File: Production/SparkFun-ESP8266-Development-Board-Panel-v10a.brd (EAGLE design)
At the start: 192.3 x 198.1 mm, 1515 parts, among them J1 DNP, J10 DNP, J11 DNP, J12 DNP, J13 DNP, J14 DNP, J15 DNP, J16 DNP, J17 DNP, J18 DNP, J19 DNP, J2 DNP, J20 DNP, J21 DNP, J3 DNP, J4 DNP, J5 DNP, J6 DNP, J7 DNP, J8 DNP, J9 DNP, Q1 2.5A/30V, Q10 2.5A/30V, Q11 2.5A/30V, Q12 2.5A/30V, Q13 2.5A/30V, Q14 2.5A/30V, Q15 2.5A/30V, Q16 2.5A/30V, Q17 2.5A/30V, Q18 2.5A/30V, Q19 2.5A/30V, Q2 2.5A/30V, Q20 2.5A/30V, Q21 2.5A/30V, Q3 2.5A/30V, Q4 2.5A/30V, Q5 2.5A/30V, Q6 2.5A/30V, Q7 2.5A/30V, Q8 2.5A/30V, Q9 2.5A/30V, U1 ESP8266, U10 ATECC108-MAHDA, U100 AT25SF041-SOIC8, U101 ATECC108-MAHDA, U102 MCP73831, U103 AP2112K-3.3V, U104 TMP1021:1, U105 TSL2561FN, U106 ESP8266, U107 AT25SF041-SOIC8, U108 ATECC108-MAHDA, U109 MCP73831, U11 MCP73831, U110 AP2112K-3.3V, U111 TMP1021:1, U112 TSL2561FN, U113 ESP8266, U114 AT25SF041-SOIC8, U115 ATECC108-MAHDA, U116 MCP73831, U117 AP2112K-3.3V, U118 TMP1021:1, U119 TSL2561FN, U12 AP2112K-3.3V, U120 ESP8266, U121 AT25SF041-SOIC8, U122 ATECC108-MAHDA, U123 MCP73831, U124 AP2112K-3.3V, U125 TMP1021:1, U126 TSL2561FN, U127 ESP8266, U128 AT25SF041-SOIC8, U129 ATECC108-MAHDA, U13 TMP1021:1, U130 MCP73831, U131 AP2112K-3.3V, U132 TMP1021:1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

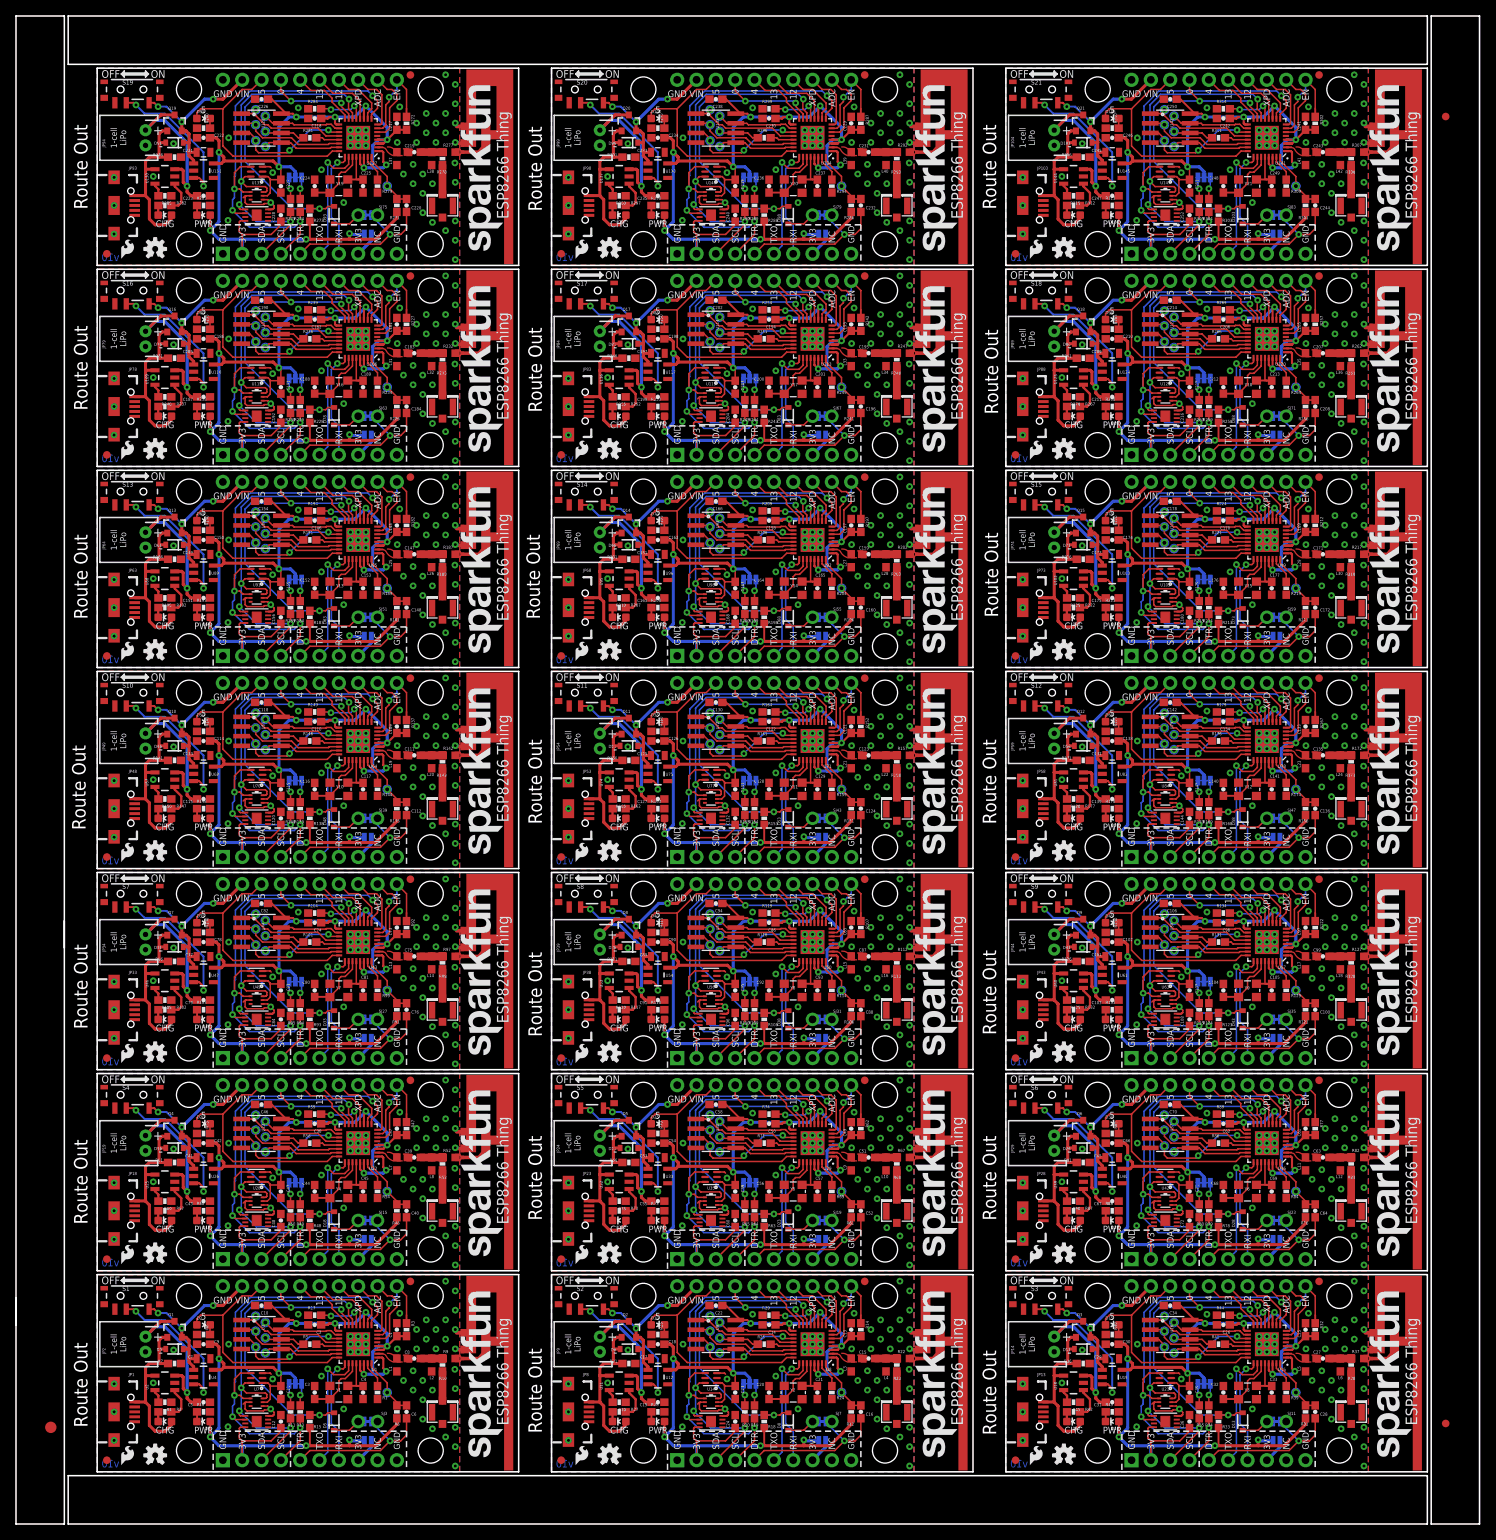
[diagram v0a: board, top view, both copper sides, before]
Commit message: Fix Silkscreen and Copper Width 0 Issue
- Replace Silkscreen for SparkFun, SFE Flame, OSH logo, and RF antenna on individual board and panel with current packages from the SparkFun Eagle Library. By having a defined width for the silkscreen/copper (instead of a "0" width), the CAM job does not generate an "infinite" amount of lines for the polygon => [ [https://learn.sparkfun.com/tutorials/importing-custom-images-into-eagle/#method-1-svg-to-polygon](https://learn.sparkfun.com/tutorials/importing-custom-images-into-eagle/#method-1-svg-to-polygon) ].
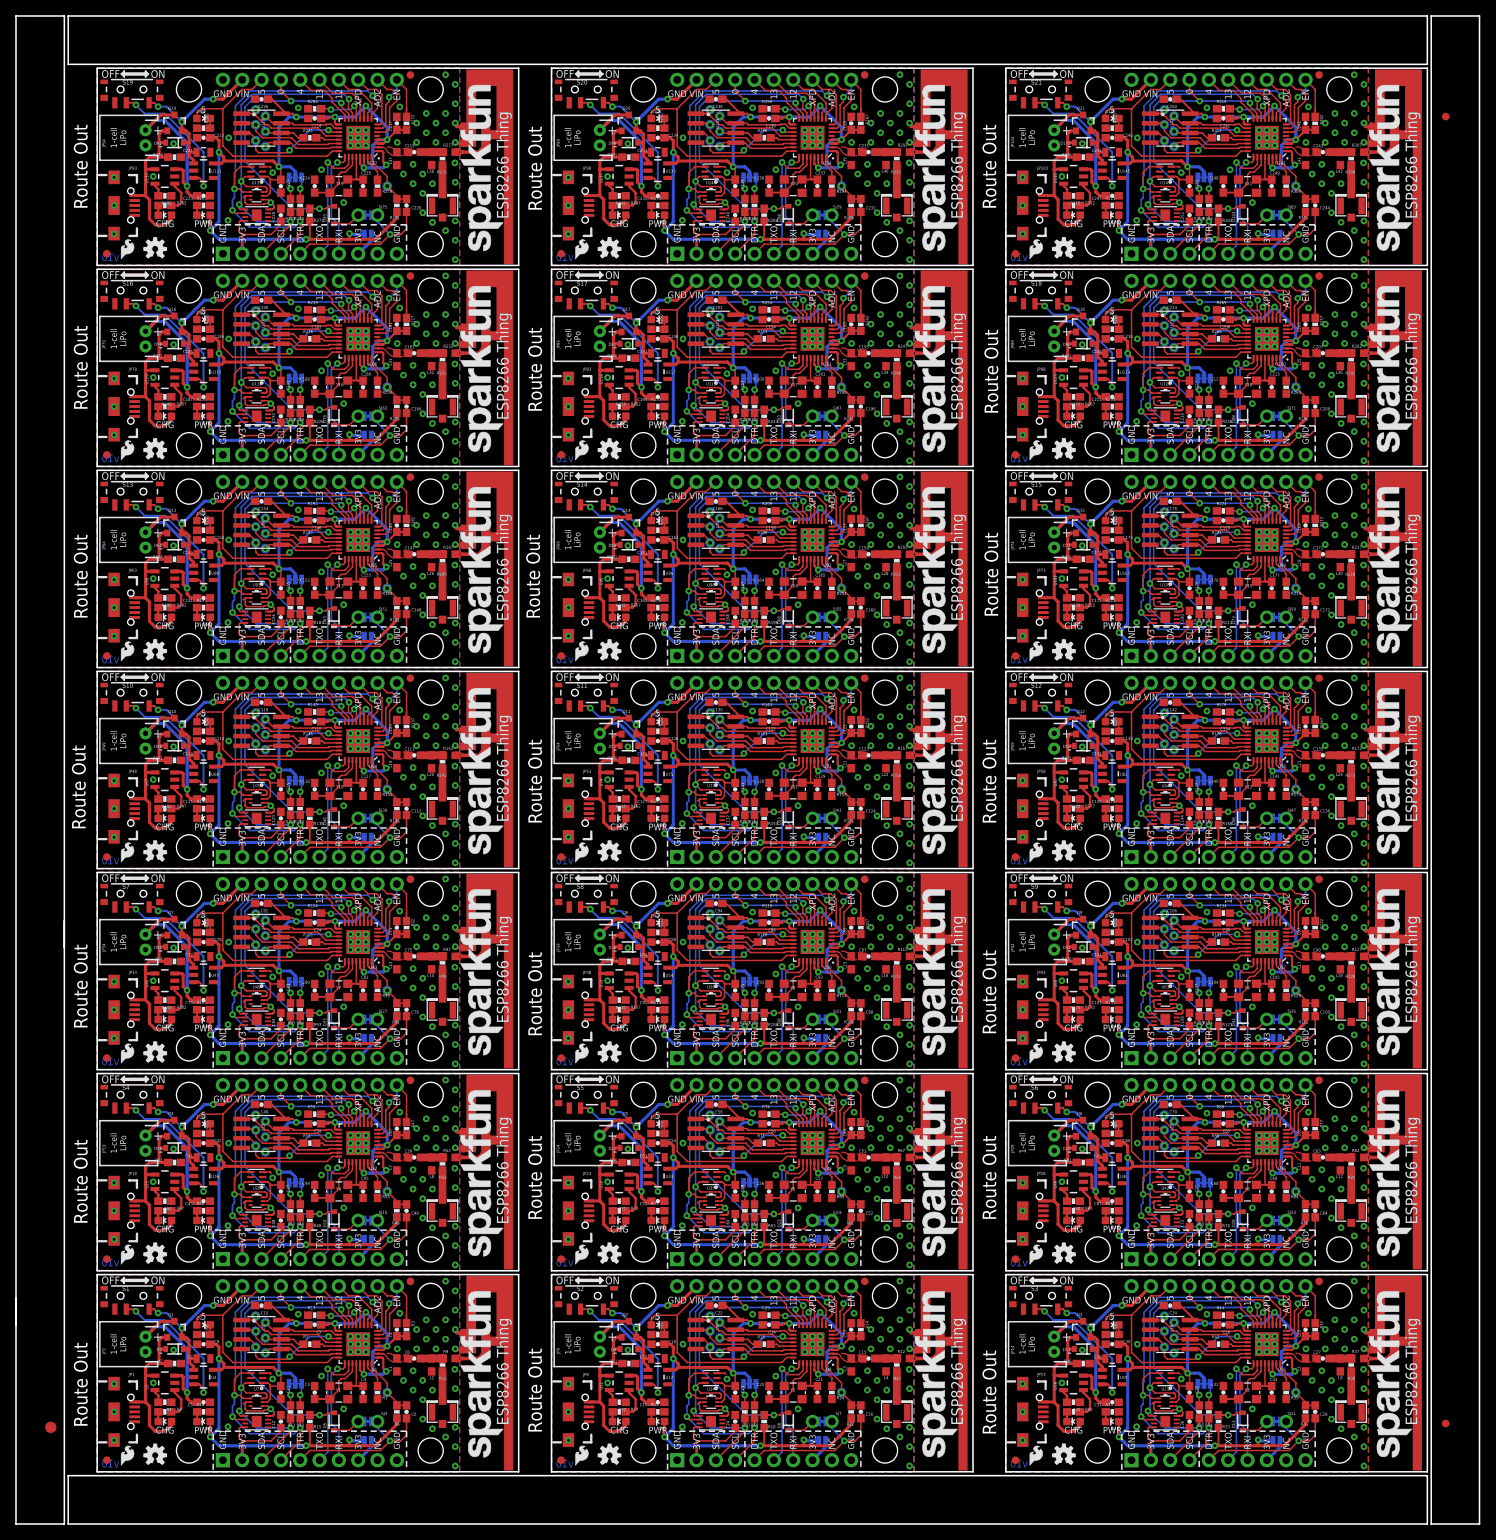
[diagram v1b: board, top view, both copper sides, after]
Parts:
- E1, E10, E11, E12, E13, E14, E15, E16, E17, E18, E19, E2, E20, E21, E3, E4, E5, E6, E7, E8, E9: device esp8266-development-board:TRACE_ANTENNA_2.4GHZ_25.7MM -> SparkFun-RF:TRACE_ANTENNA_2.4GHZ_25.7MM
